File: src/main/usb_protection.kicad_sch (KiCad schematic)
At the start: 4 parts, among them J501 Conn_01x03, U104 TPD3S014

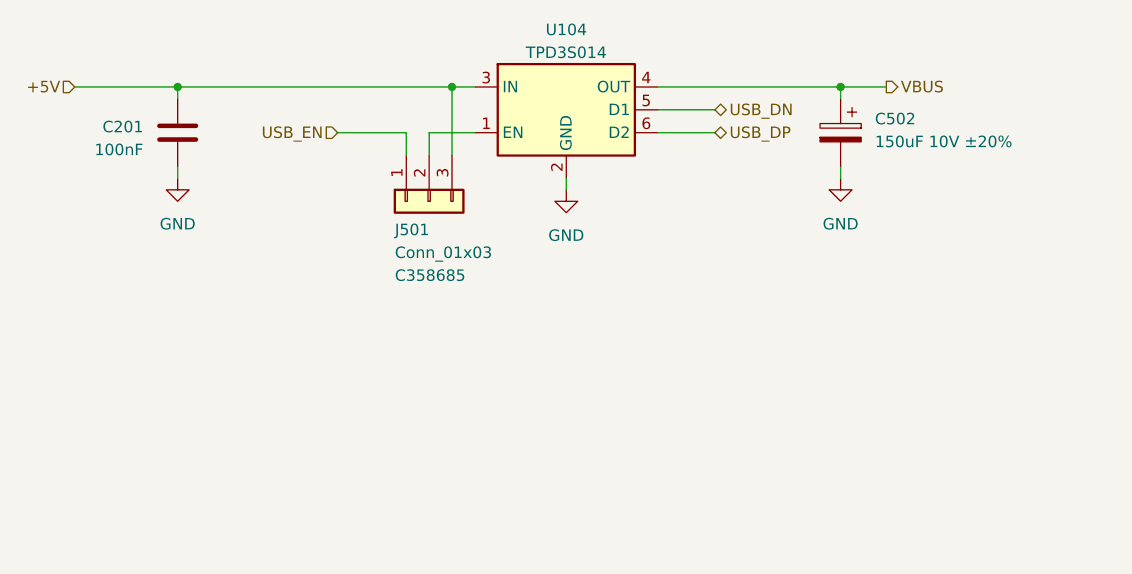
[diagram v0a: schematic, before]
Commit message: Additions and fixes:
Add:
- Add power rail LED status indicators
- Buffered LED on ETH_LINK
- GPIO14 and GPIO12 on header
- GPIO14 5V buffered output on header
- Testpoints for GPIO0 and ESP32_ENABLE pin
- Reset and Boot switches
- ESP PWR selector switch
- USB Type-C PD input (5V) for ESP32
- 1.1A Fuse for USB PD input
- Add spot for BIOS battery on silk
- Add silkscreen default jumper marking
- Add GPIO39 external pullup to 3V3
- Add pulldown to PWR_BUTTON (GPIO15)
- Add silkscreen github link

Fixes:
- Clarify things on silk
- Make pinout compatible with USB-UART boards
  - Move GPI0 and ENABLE to testpoints
- Silkscreen alignment fixes

Removed:
- 3 APA102 LEDs
- Remove JP201
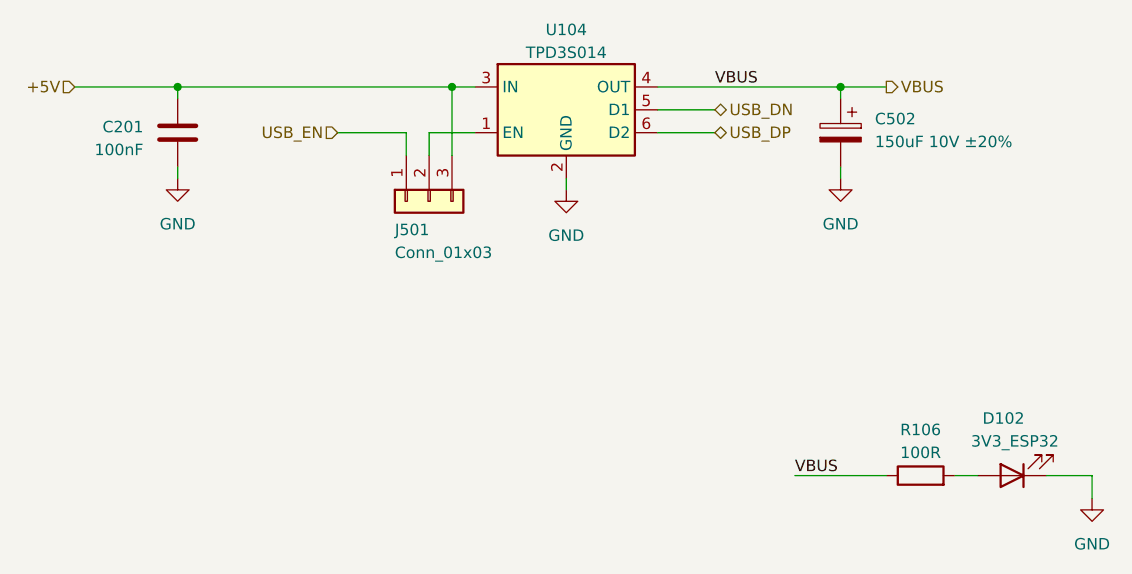
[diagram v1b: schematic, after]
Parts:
- added D102: 3V3_ESP32, LED_SMD:LED_0603_1608Metric, symbol Device:LED
- added R106: 100R, Resistor_SMD:R_0402_1005Metric, symbol Device:R
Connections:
- net GND: now also D102.1 (K)
- net VBUS: now also R106.1
- new net: D102.2 (A), R106.2
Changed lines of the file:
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@@
   (title_block
     (title "ODROID H3(+) mITX adapter")
-    (date "2023-05-07")
-    (rev "1.0.0")
+    (date "2023-08-13")
+    (rev "1.1.0")
   )
   (junction (at 184.15 80.01) (diameter 0) (color 0 0 0 0)
@@
     (stroke (width 0) (type default))
   )
+  (wire (pts (xy 179.07 123.19) (xy 189.23 123.19))
+    (stroke (width 0) (type default))
+  )
   (wire (pts (xy 135.89 87.63) (xy 135.89 85.09))
     (stroke (width 0) (type default))
@@
     (stroke (width 0) (type default))
   )
+  (wire (pts (xy 199.39 123.19) (xy 196.85 123.19))
+    (stroke (width 0) (type default))
+  )
   (wire (pts (xy 184.15 80.01) (xy 189.23 80.01))
     (stroke (width 0) (type default))
   )
+  (wire (pts (xy 207.01 123.19) (xy 212.09 123.19))
+    (stroke (width 0) (type default))
+  )
   (wire (pts (xy 184.15 88.9) (xy 184.15 90.17))
     (stroke (width 0) (type default))
@@
     (stroke (width 0) (type default))
   )
+  (wire (pts (xy 212.09 123.19) (xy 212.09 125.73))
+    (stroke (width 0) (type default))
+  )
   (wire (pts (xy 140.97 80.01) (xy 143.51 80.01))
     (stroke (width 0) (type default))
+  )
+  (label "VBUS" (at 179.07 123.19 0) (fields_autoplaced)
+    (effects (font (size 1.27 1.27)) (justify left bottom))
+  )
+  (label "VBUS" (at 170.18 80.01 0) (fields_autoplaced)
+    (effects (font (size 1.27 1.27)) (justify left bottom))
   )
   (hierarchical_label "+5V" (shape input) (at 99.06 80.01 180) (fields_autoplaced)
@@
     )
     (property "LCSC" "C358685" (at 134.62 100.965 90)
-      (effects (font (size 1.27 1.27)) (justify right))
+      (effects (font (size 1.27 1.27)) (justify right) hide)
     )
     (pin "1")
@@
     )
   )
+  (symbol (lib_id "Device:R") (at 193.04 123.19 90) (unit 1)
+    (in_bom yes) (on_board yes) (dnp no)
+    (property "Reference" "R106" (at 193.04 118.11 90)
+      (effects (font (size 1.27 1.27)))
+    )
+    (property "Value" "100R" (at 193.04 120.65 90)
+      (effects (font (size 1.27 1.27)))
+    )
+    (property "Footprint" "Resistor_SMD:R_0402_1005Metric" (at 193.04 124.968 90)
+      (effects (font (size 1.27 1.27)) hide)
+    )
+    (property "Datasheet" "~" (at 193.04 123.19 0)
+      (effects (font (size 1.27 1.27)) hide)
+    )
+    (property "LCSC" "C25076" (at 193.04 123.19 90)
+      (effects (font (size 1.27 1.27)) hide)
+    )
+    (pin "1")
+    (pin "2")
+    (instances
+      (project "main"
+        (path "/2a886fd6-2916-429a-83b7-5c78dd9fc58d"
+          (reference "R106") (unit 1)
+        )
+        (path "/2a886fd6-2916-429a-83b7-5c78dd9fc58d/d2b75146-6fcd-4cec-8c17-a2810b6898f8"
+          (reference "R302") (unit 1)
+        )
+        (path "/2a886fd6-2916-429a-83b7-5c78dd9fc58d/5dba0873-0deb-4e19-8a67-60039d1616d3"
+          (reference "R203") (unit 1)
+        )
+        (path "/2a886fd6-2916-429a-83b7-5c78dd9fc58d/f7a41b07-1203-4fbe-a050-976428b6e8c1/3295fd3c-7c2e-428b-928b-e5c9eb9e9af2"
+          (reference "R501") (unit 1)
+        )
+        (path "/2a886fd6-2916-429a-83b7-5c78dd9fc58d/f7a41b07-1203-4fbe-a050-976428b6e8c1/181941b7-0d2d-4406-8bab-aaa9c10a9ba8"
+          (reference "R601") (unit 1)
+        )
+        (path "/2a886fd6-2916-429a-83b7-5c78dd9fc58d/f7a41b07-1203-4fbe-a050-976428b6e8c1/735d1b9d-8c9f-485f-b4f3-dab2c75d1545"
+          (reference "R701") (unit 1)
+        )
+      )
+    )
+  )
   (symbol (lib_id "Device:C_Polarized") (at 184.15 85.09 0) (mirror y) (unit 1)
     (in_bom yes) (on_board yes) (dnp no)
@@
     )
   )
+  (symbol (lib_id "power:GND") (at 212.09 125.73 0) (mirror y) (unit 1)
+    (in_bom yes) (on_board yes) (dnp no) (fields_autoplaced)
+    (property "Reference" "#PWR0105" (at 212.09 132.08 0)
+      (effects (font (size 1.27 1.27)) hide)
+    )
+    (property "Value" "GND" (at 212.09 130.81 0)
+      (effects (font (size 1.27 1.27)))
+    )
+    (property "Footprint" "" (at 212.09 125.73 0)
+      (effects (font (size 1.27 1.27)) hide)
+    )
+    (property "Datasheet" "" (at 212.09 125.73 0)
+      (effects (font (size 1.27 1.27)) hide)
+    )
+    (pin "1")
+    (instances
+      (project "main"
+        (path "/2a886fd6-2916-429a-83b7-5c78dd9fc58d"
+          (reference "#PWR0105") (unit 1)
+        )
+        (path "/2a886fd6-2916-429a-83b7-5c78dd9fc58d/5dba0873-0deb-4e19-8a67-60039d1616d3"
+          (reference "#PWR0203") (unit 1)
+        )
+        (path "/2a886fd6-2916-429a-83b7-5c78dd9fc58d/f7a41b07-1203-4fbe-a050-976428b6e8c1"
+          (reference "#PWR0406") (unit 1)
+        )
+        (path "/2a886fd6-2916-429a-83b7-5c78dd9fc58d/f7a41b07-1203-4fbe-a050-976428b6e8c1/3295fd3c-7c2e-428b-928b-e5c9eb9e9af2"
+          (reference "#PWR0504") (unit 1)
+        )
+        (path "/2a886fd6-2916-429a-83b7-5c78dd9fc58d/f7a41b07-1203-4fbe-a050-976428b6e8c1/181941b7-0d2d-4406-8bab-aaa9c10a9ba8"
+          (reference "#PWR0604") (unit 1)
+        )
+        (path "/2a886fd6-2916-429a-83b7-5c78dd9fc58d/f7a41b07-1203-4fbe-a050-976428b6e8c1/735d1b9d-8c9f-485f-b4f3-dab2c75d1545"
+          (reference "#PWR0704") (unit 1)
+        )
+      )
+    )
+  )
   (symbol (lib_id "Device:C") (at 110.49 85.09 0) (mirror y) (unit 1)
     (in_bom yes) (on_board yes) (dnp no)
@@
         )
       )
+    )
+  )
+  (symbol (lib_id "Device:LED") (at 203.2 123.19 180) (unit 1)
+    (in_bom yes) (on_board yes) (dnp no)
+    (property "Reference" "D102" (at 202.2475 116.84 0)
+      (effects (font (size 1.27 1.27)))
+    )
+    (property "Value" "3V3_ESP32" (at 203.5175 119.38 0)
+      (effects (font (size 1.27 1.27)))
+    )
+    (property "Footprint" "LED_SMD:LED_0603_1608Metric" (at 203.2 123.19 0)
+      (effects (font (size 1.27 1.27)) hide)
+    )
+    (property "Datasheet" "https://datasheet.lcsc.com/lcsc/1810201530_BrtLed-Bright-LED-Elec-BL-HKC36G-AV-TRB_C165981.pdf" (at 203.2 123.19 0)
+      (effects (font (size 1.27 1.27)) hide)
+    )
+    (property "LCSC" "C165981" (at 203.2 123.19 0)
+      (effects (font (size 1.27 1.27)) hide)
+    )
+    (pin "1")
+    (pin "2")
+    (instances
+      (project "main"
+        (path "/2a886fd6-2916-429a-83b7-5c78dd9fc58d"
+          (reference "D102") (unit 1)
+        )
+        (path "/2a886fd6-2916-429a-83b7-5c78dd9fc58d/d2b75146-6fcd-4cec-8c17-a2810b6898f8"
+          (reference "D302") (unit 1)
+        )
+        (path "/2a886fd6-2916-429a-83b7-5c78dd9fc58d/5dba0873-0deb-4e19-8a67-60039d1616d3"
+          (reference "D204") (unit 1)
+        )
+        (path "/2a886fd6-2916-429a-83b7-5c78dd9fc58d/f7a41b07-1203-4fbe-a050-976428b6e8c1/3295fd3c-7c2e-428b-928b-e5c9eb9e9af2"
+          (reference "D501") (unit 1)
+        )
+        (path "/2a886fd6-2916-429a-83b7-5c78dd9fc58d/f7a41b07-1203-4fbe-a050-976428b6e8c1/181941b7-0d2d-4406-8bab-aaa9c10a9ba8"
+          (reference "D601") (unit 1)
+        )
+        (path "/2a886fd6-2916-429a-83b7-5c78dd9fc58d/f7a41b07-1203-4fbe-a050-976428b6e8c1/735d1b9d-8c9f-485f-b4f3-dab2c75d1545"
+          (reference "D701") (unit 1)
+        )
+      )
